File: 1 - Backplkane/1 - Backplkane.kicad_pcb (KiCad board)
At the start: 2 copper layers, 154.9 x 124.5 mm, 37 parts, among them J1 BUS 1, J10 EXTENDED BUS, J11 5V DC, J2 BUS 2, J3 BUS 3, J4 BUS 4, J5 BUS 5, J6 BUS 6, J7 BUS 7, J8 BUS 8, J9 BASIC BUS, U1 LD1117AV33

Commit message: Converted files from version 6 to 7 of KiCad
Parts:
- added REF**: OSHW-Logo2_14.6x12mm_SilkScreen, Symbol:OSHW-Logo2_14.6x12mm_SilkScreen, F.Cu at (92.7, 43.2)
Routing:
- net /D4: track 202.4 -> 202.9 mm
- net /D1: track 213.2 -> 213.7 mm
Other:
- board text added: "8-slot 62-pin Edge Connector Backplane"
- board text added: "Designed by Frédéric Segard"
- board text added: "Homebrew Project"
- board text added: "JLCJLCJLC"
- board text added: "NKK M2012S2A2W30"
- board text added: "youtube.com/@microhobbyist github.com/fredericsegard"
- board text removed: "1"
- board text removed: "Backplane Edition"
- board text removed: "Designed by Frédéric Segard a.k.a: The Micro Hobbyist"
- board text removed: "Z80 Homebrew"

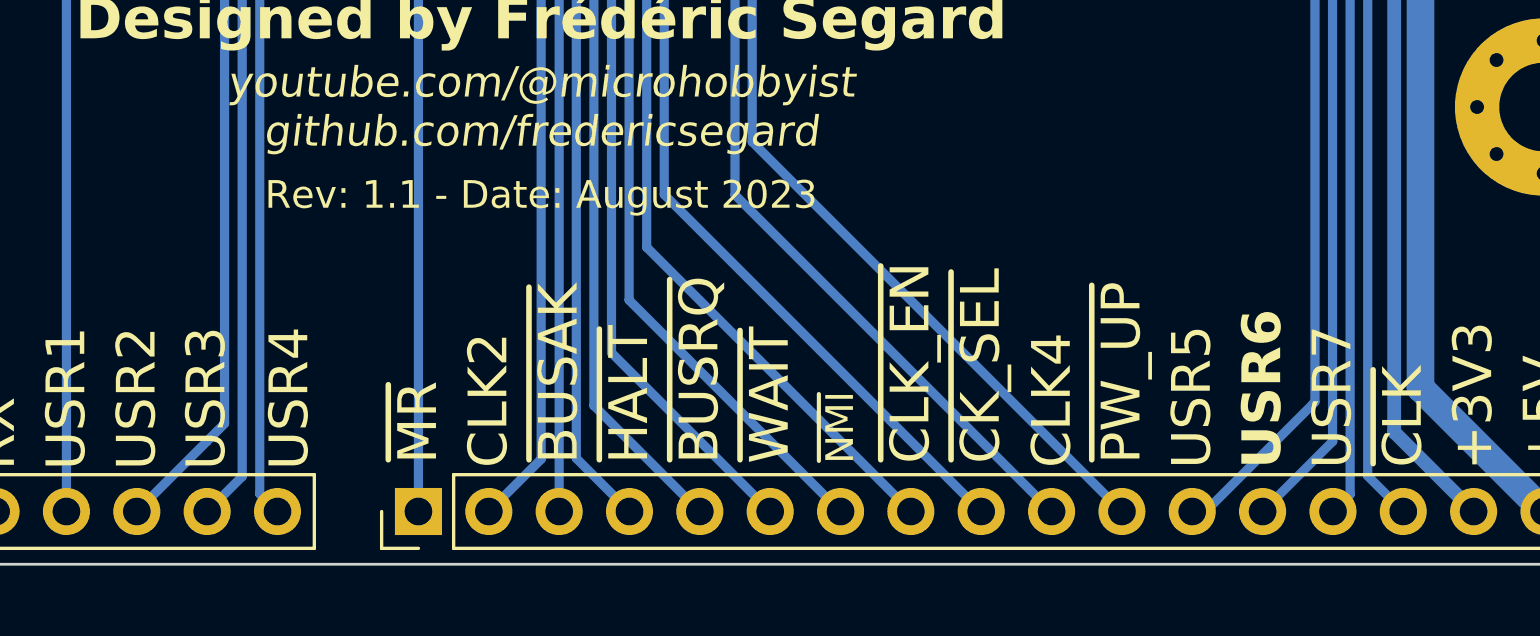
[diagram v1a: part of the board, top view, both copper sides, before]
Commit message: Added serial card, still needs work
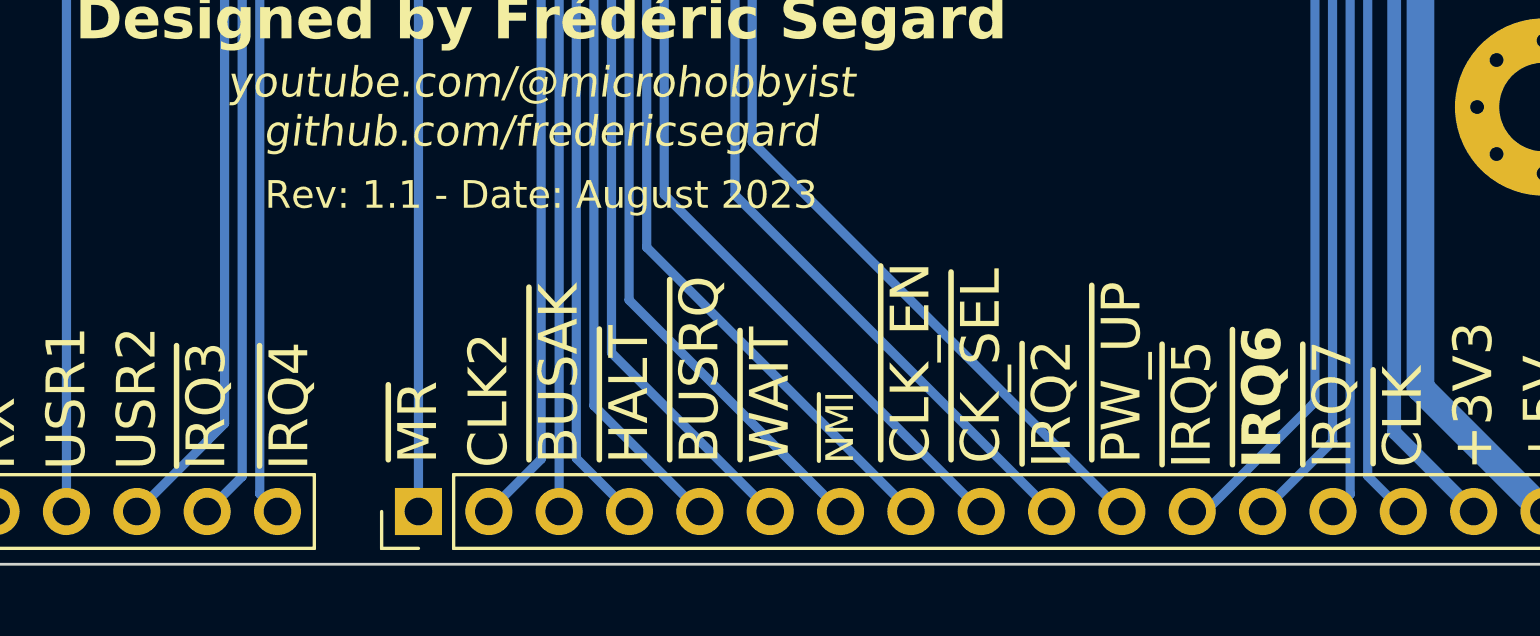
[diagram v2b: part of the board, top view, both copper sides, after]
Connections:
- net /CLK4 renamed /~{IRQ}2
- net /USER3 renamed /~{IRQ}3
- net /USER4 renamed /~{IRQ}4
- net /USER5 renamed /~{IRQ}5
- net /USER6 renamed /~{IRQ}6
- net /USER7 renamed /~{IRQ}7
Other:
- board text added: "~{IRQ2}"
- board text added: "~{IRQ3}"
- board text added: "~{IRQ4}"
- board text added: "~{IRQ5}"
- board text added: "~{IRQ6}"
- board text added: "~{IRQ7}"
- board text removed: "CLK4"
- board text removed: "USR3"
- board text removed: "USR4"
- board text removed: "USR5"
- board text removed: "USR6"
- board text removed: "USR7"
